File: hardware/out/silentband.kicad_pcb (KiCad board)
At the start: 4 copper layers, 68 x 46 mm, 107 parts, among them J1 Electrodes, J2 IMU, J3 USB-C, J4 LiPo 1S, Q1 AO3401A, Q2 AO3401A, SW1 RESET, SW2 BOOT, SW3 POWER, U1 ADS1298IPAGR, U2 ADS1298IPAGR, U3 ESP32-S3-WROOM-1-N8, U4 USBLC6-2SC6, U5 MCP73831T-2ACI/OT, U6 AP2112K-3.3TRG1, U7 LP5907MFX-3.0/NOPB

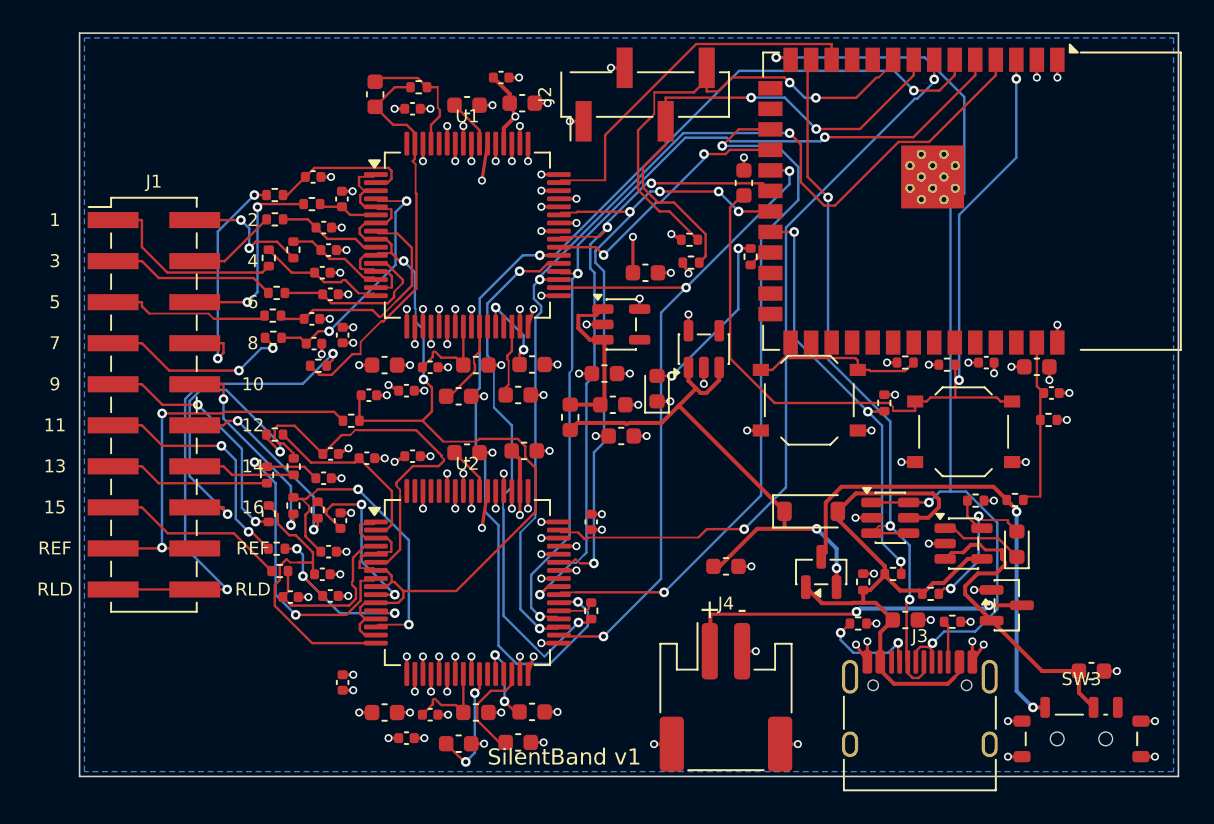
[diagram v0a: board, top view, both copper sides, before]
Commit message: Apply Fable review: slave reset timing, tantalum VCAP1, clocks on F.Cu, low-battery stop
Co-Authored-By: Claude <noreply@anthropic.com>
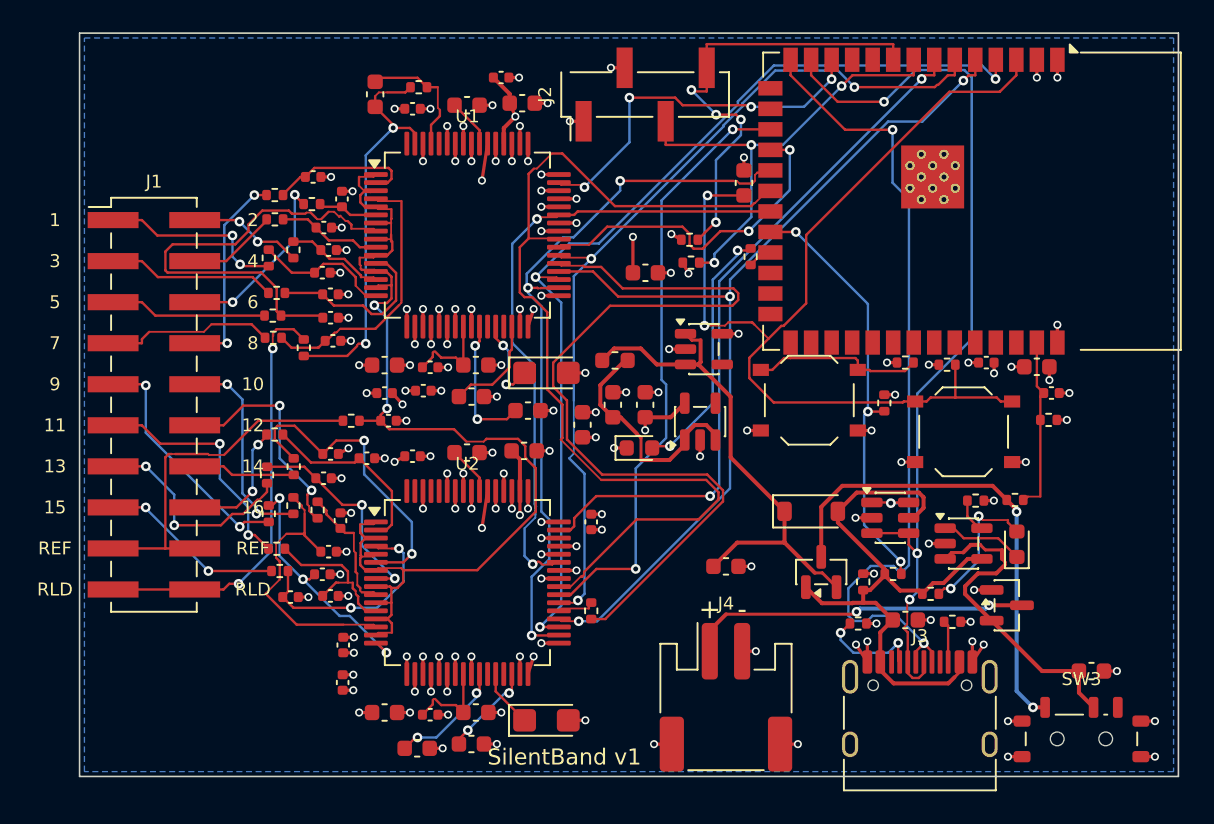
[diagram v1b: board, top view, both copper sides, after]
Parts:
- C20, C32: footprint Capacitor_SMD:C_0603_1608Metric -> Capacitor_Tantalum_SMD:CP_EIA-3216-18_Kemet-A
- moved U7 7.74 mm to (38.4, 24.0), turned to 90 degrees
- moved C37 5.24 mm to (16.3, 40.2), turned to 90 degrees
- moved FB1 4.48 mm to (33.1, 20.3), turned to 0 degrees
- moved C27 4.43 mm to (18.9, 22.3), turned to 0 degrees
- moved C23 4.38 mm to (27.8, 23.4)
- moved D1 3.83 mm to (34.6, 25.7), turned to 0 degrees
- moved C53 3.45 mm to (31.1, 24.2), turned to 90 degrees
- moved C21 2.89 mm to (24.2, 22.5)
- moved C33 2.89 mm to (24.2, 44.0)
- moved C35 2.58 mm to (20.9, 44.3)
- moved C52 2.44 mm to (35.0, 23.0), turned to 90 degrees
- moved C39 2.32 mm to (16.3, 37.9)
- moved C17 1.99 mm to (19.1, 24.0)
- moved R20 1.44 mm to (13.9, 19.5), turned to 90 degrees
- moved C7 1.18 mm to (15.7, 19.0)
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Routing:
- net CLK_M: track 33.1 -> 53.3 mm, vias 2 -> 0
- net SCLK: track 41.2 -> 61.0 mm, vias 3 -> 0
- net START: track 70.3 -> 54.8 mm
- net IN5: track 14.4 -> 28.5 mm
- net EL16: track 19.4 -> 7.86 mm
- net USB_DN: track 46.3 -> 57.0 mm
- net EN: track 53.8 -> 62.4 mm
- net IN13: track 21.3 -> 13.4 mm
- net REF: track 75.7 -> 68.4 mm
- net CS2: track 45.0 -> 37.7 mm
- net USB_DP: track 60.4 -> 54.1 mm
- net IN14: track 24.8 -> 19.7 mm, vias 0 -> 2
- net CS1: track 16.2 -> 21.0 mm
- net LED_A: track 11.3 -> 15.8 mm
- net RLD_E: track 31.2 -> 26.6 mm
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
